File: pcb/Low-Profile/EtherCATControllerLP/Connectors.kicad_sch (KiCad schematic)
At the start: 20 parts, among them J1 FH41-40S-0.5SH_05_, J2 Right Angle 1x4, J3 Conn_01x04_Socket, J4 TYPE-C-31-M-12

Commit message: checkpoint
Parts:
- J1: LCSC Part # (none) -> C596805; LCSC Part Number C596805 -> (none)
- J2: LCSC Part # (none) -> C91552; LCSC Part Number C91552 -> (none)
- J4: LCSC Part # (none) -> C165948; LCSC Part Number C165948 -> (none)
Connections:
- net VDD is gone; now on net VCC: JP1.2 (B)
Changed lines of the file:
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@@
 			)
 		)
-		(property "LCSC Part Number" "C165948"
+		(property "LCSC Part #" "C165948"
 			(at 73.66 157.48 0)
 			(effects
@@
 			)
 		)
-		(property "LCSC Part Number" "C596805"
+		(property "LCSC Part #" "C596805"
 			(at 209.55 86.36 0)
 			(effects
@@
 			)
 		)
-		(property "LCSC Part Number" " C91552"
+		(property "LCSC Part #" " C91552"
 			(at 114.3 125.984 0)
 			(effects
@@
 			)
 		)
-		(property "Value" "VDD"
-			(at 106.68 34.29 0)
-			(effects
-				(font
-					(size 1.27 1.27)
-				)
-			)
-		)
+		(property "Value" "VCC"
+			(at 109.22 38.0999 0)
+			(effects
+				(font
+					(size 1.27 1.27)
+				)
+				(justify left)
+			)
+		)

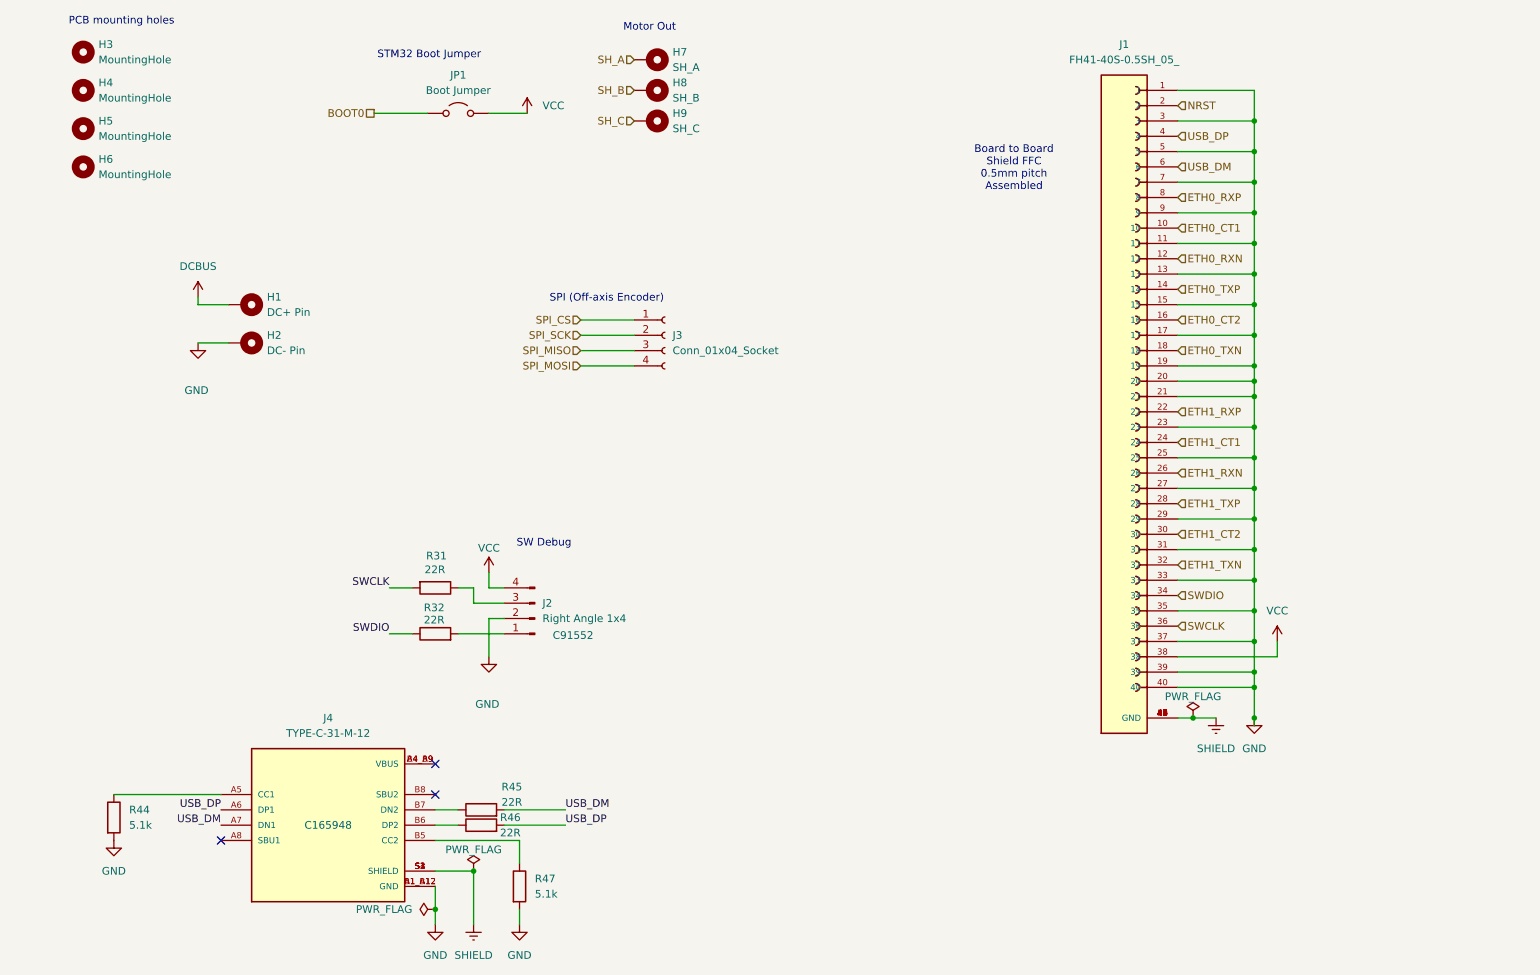
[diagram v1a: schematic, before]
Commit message: Checkpoint changes before switching to XMC4800
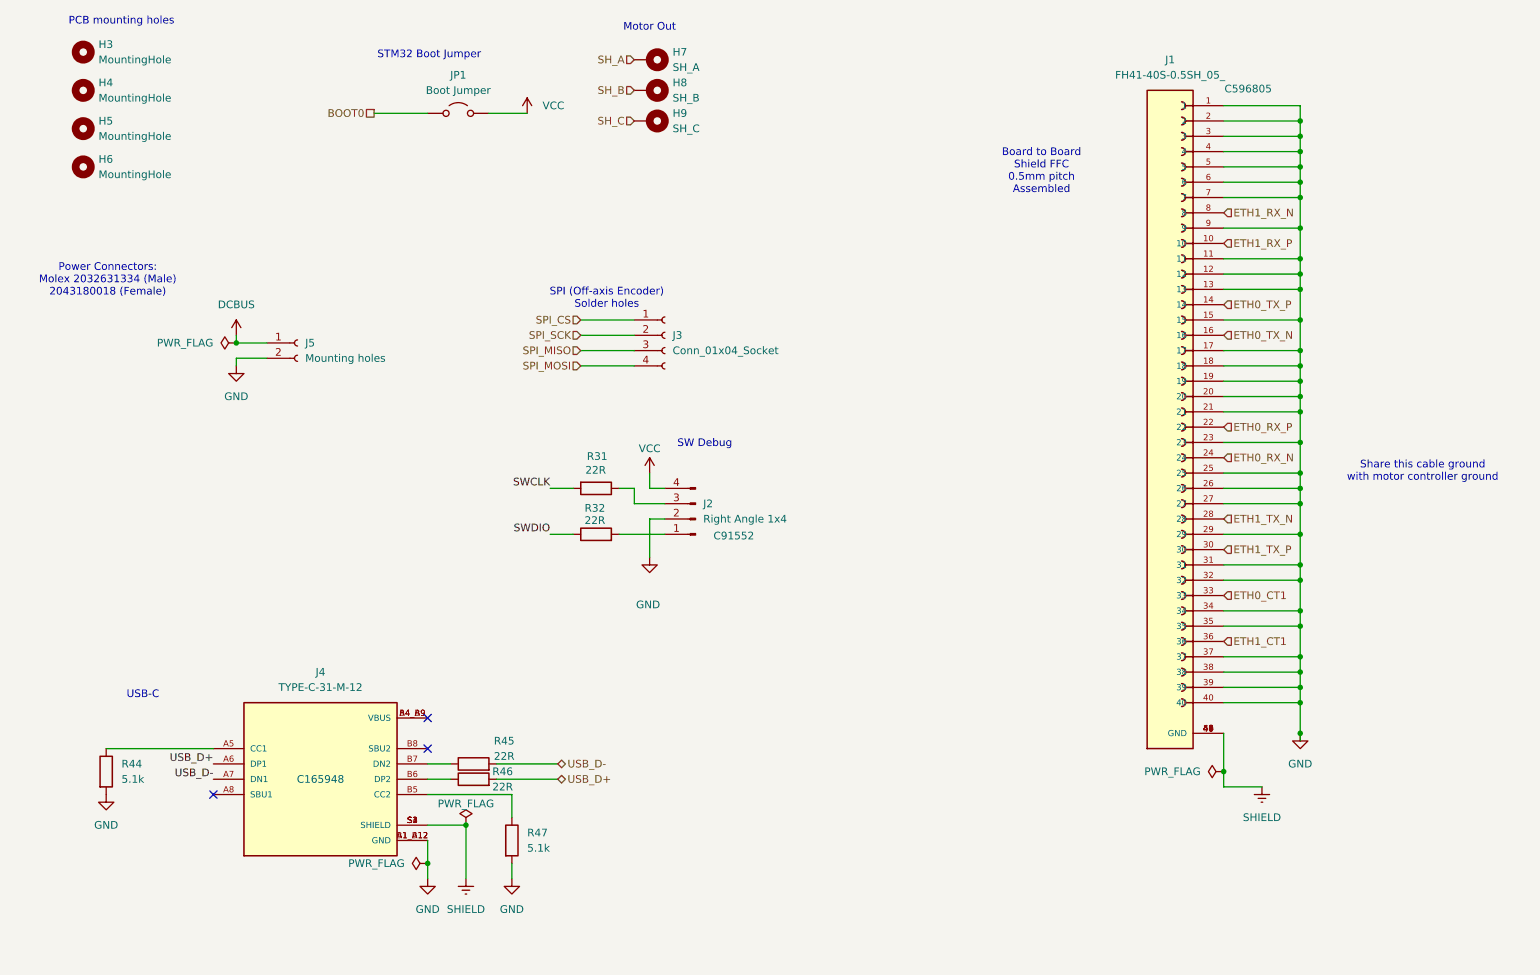
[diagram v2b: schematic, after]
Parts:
- removed H1: DC+ Pin, symbol Mechanical:MountingHole_Pad
- removed H2: DC- Pin, symbol Mechanical:MountingHole_Pad
- added J5: Mounting holes, holes:Dual Post, symbol Connector:Conn_01x02_Socket
- J1: footprint FH41-40S-0.5SH_05_:HRS_FH41-40S-0.5SH_05_ -> FH41:HRS_FH41-40S-0.5SH_05_
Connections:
- net ETH0_RXN is gone; now on net GND: J1.12
- net ETH0_TXN is gone; now on net GND: J1.18
- net ETH1_RXN is gone; now on net GND: J1.26
- net ETH1_TXN is gone; now on net GND: J1.32
- net NRST is gone; now on net GND: J1.2
- net DCBUS: now also J5.1 (Pin_1)
- net ETH0_CT1: now also J1.33; no longer J1.10
- net ETH1_CT1: now also J1.36; no longer J1.24
- net GND: now also J1.34, J1.38, J1.4, J1.6, J5.2 (Pin_2); no longer J1.33
- net SWCLK: no longer J1.36
- net SWDIO: no longer J1.34
- net VCC: no longer J1.38
- net ETH0_CT2 renamed ETH0_TX_N
- net ETH0_RXP renamed ETH1_RX_N
- net ETH0_TXP renamed ETH0_TX_P
- net ETH1_CT2 renamed ETH1_TX_P
- net ETH1_RXP renamed ETH0_RX_P
- net ETH1_TXP renamed ETH1_TX_N
- net USB_DM renamed USB_D-
- net USB_D-: no longer J1.6
- net USB_DP renamed USB_D+
- net USB_D+: no longer J1.4
- new net ETH0_RX_N: J1.24
- new net ETH1_RX_P: J1.10
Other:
- note added: "Power Connectors: Molex 2032631334 (Male) 2043180018 (Female)"
- note added: "SPI (Off-axis Encoder) Solder holes"
- note added: "Share this cable ground with motor controller ground"
- note added: "USB-C"
- note removed: "SPI (Off-axis Encoder)"
- moved on the sheet: J2, J4, R31, R32, R44, R45, R46, R47

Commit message: Finished new 2+2 IOboard
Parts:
- R31, R32, R45, R46: LCSC Part # (none) -> C107701
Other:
- note added: "Power connectors using Samtec UMPT-02/UMPS-02"
- note removed: "Power Connectors: Molex 2032631334 (Male) 2043180018 (Female)"
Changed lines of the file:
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@@
+		)
+	)
+	(text "Power connectors using\nSamtec UMPT-02/UMPS-02"
+		(exclude_from_sim no)
+		(at 36.322 70.104 0)
+		(effects
+			(font
+				(size 1.27 1.27)
+			)
 		)
 	)
@@
 		(exclude_from_sim no)
 		(at 136.144 94.234 0)
-		(effects
-			(font
-				(size 1.27 1.27)
-			)
-		)
-	)
-	(text "Power Connectors:\nMolex 2032631334 (Male)\n2043180018 (Female)"
-		(exclude_from_sim no)
-		(at 37.084 67.056 0)
 		(effects
 			(font
@@
 			)
 		)
+		(property "LCSC Part #" "C107701"
+			(at 97.79 147.32 0)
+			(effects
+				(font
+					(size 1.27 1.27)
+				)
+				(hide yes)
+			)
+		)
 		(pin "1"
 		)
@@
 			)
 		)
+		(property "LCSC Part #" "C107701"
+			(at 118.11 101.6 0)
+			(effects
+				(font
+					(size 1.27 1.27)
+				)
+				(hide yes)
+			)
+		)
 		(pin "2"
 		)
@@
 			)
 		)
+		(property "LCSC Part #" "C107701"
+			(at 118.11 109.22 0)
+			(effects
+				(font
+					(size 1.27 1.27)
+				)
+				(hide yes)
+			)
+		)
 		(pin "1"
 		)
@@
 			(at 97.79 149.86 0)
 			(effects
+				(font
+					(size 1.27 1.27)
+				)
+				(hide yes)
+			)
+		)
+		(property "LCSC Part #" "C107701"
+			(at 97.79 149.86 0)
+			(effects

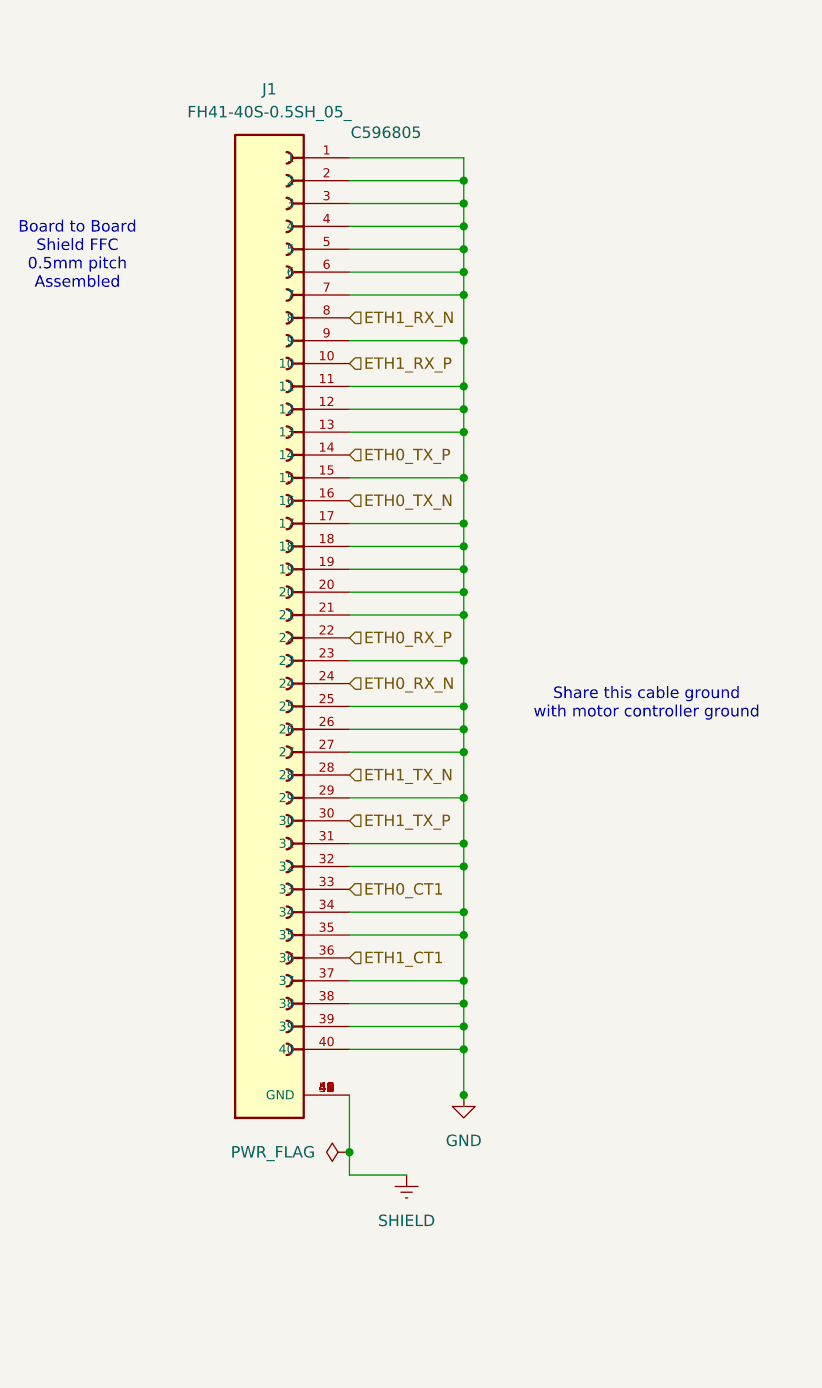
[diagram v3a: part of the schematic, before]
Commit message: Added XMC4800
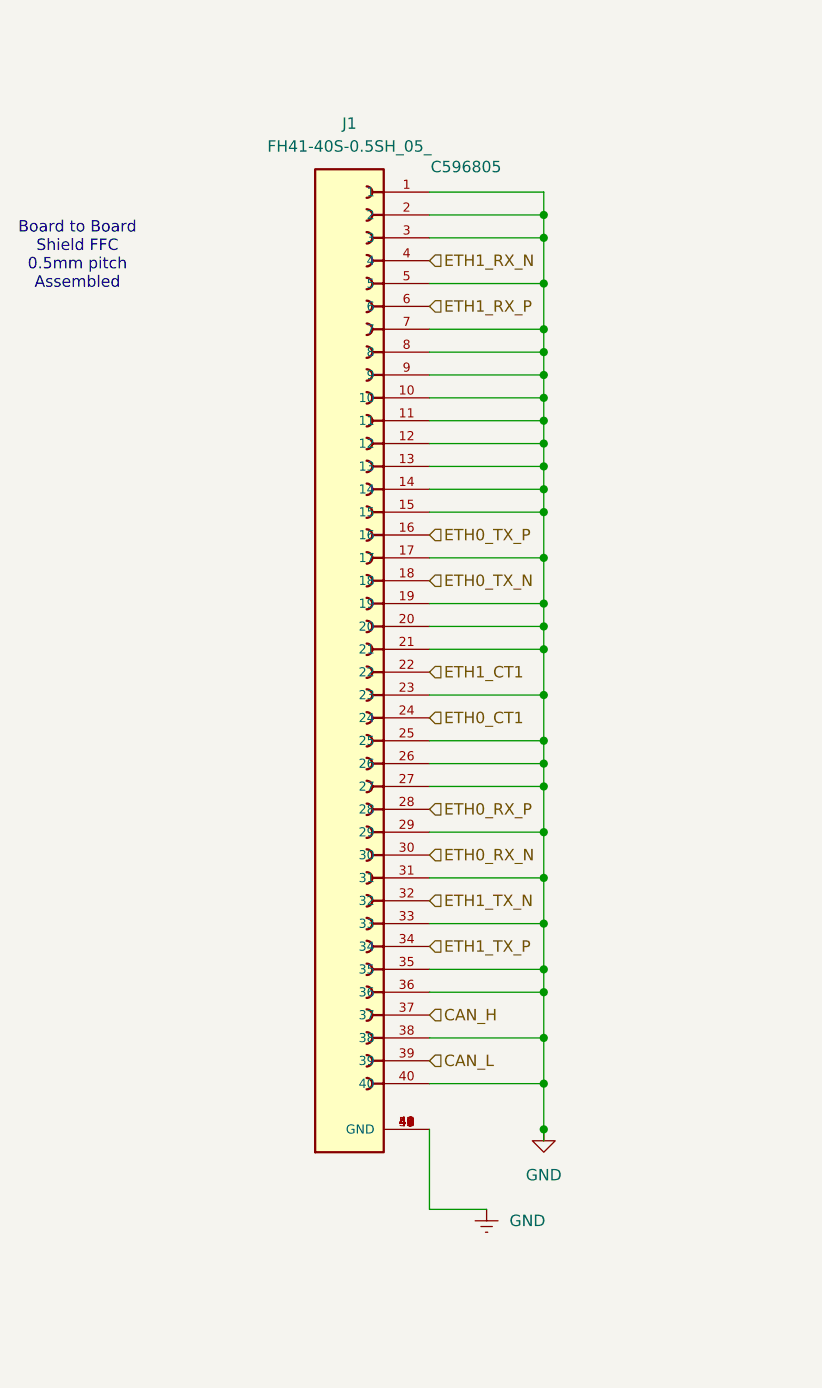
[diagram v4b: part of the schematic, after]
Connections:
- net ETH0_CT1: now also J1.24; no longer J1.33
- net ETH0_RX_N: now also J1.30; no longer J1.24
- net ETH0_RX_P: now also J1.28; no longer J1.22
- net ETH0_TX_N: now also J1.18; no longer J1.16
- net ETH0_TX_P: now also J1.16; no longer J1.14
- net ETH1_CT1: now also J1.22; no longer J1.36
- net ETH1_RX_N: now also J1.4; no longer J1.8
- net ETH1_RX_P: now also J1.6; no longer J1.10
- net ETH1_TX_N: now also J1.32; no longer J1.28
- net ETH1_TX_P: now also J1.34; no longer J1.30
- net GND: now also J1.10, J1.14, J1.33, J1.36, J1.41 (GND), J1.42 (GND), J1.43 (GND), J1.44 (GND), J1.45 (GND), J1.46 (GND), J1.47 (GND), J1.48 (GND), J1.49 (GND), J1.50 (GND), J1.8; no longer J1.18, J1.32, J1.34, J1.37, J1.39, J1.4, J1.6
- net SHIELD: no longer J1.41 (GND), J1.42 (GND), J1.43 (GND), J1.44 (GND), J1.45 (GND), J1.46 (GND), J1.47 (GND), J1.48 (GND), J1.49 (GND), J1.50 (GND)
- new net CAN_H: J1.37
- new net CAN_L: J1.39
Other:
- note removed: "Share this cable ground with motor controller ground"

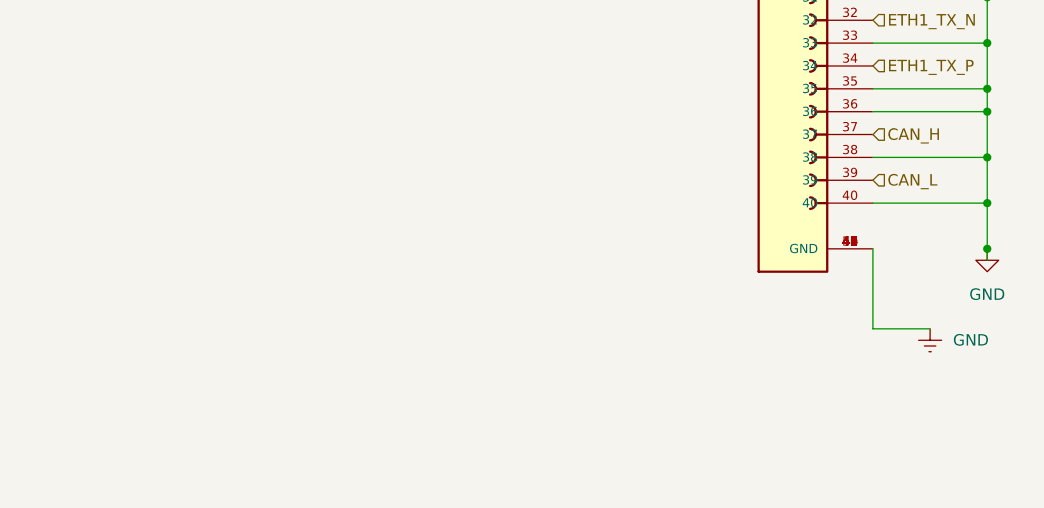
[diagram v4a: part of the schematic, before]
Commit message: Added Ethernet PHY
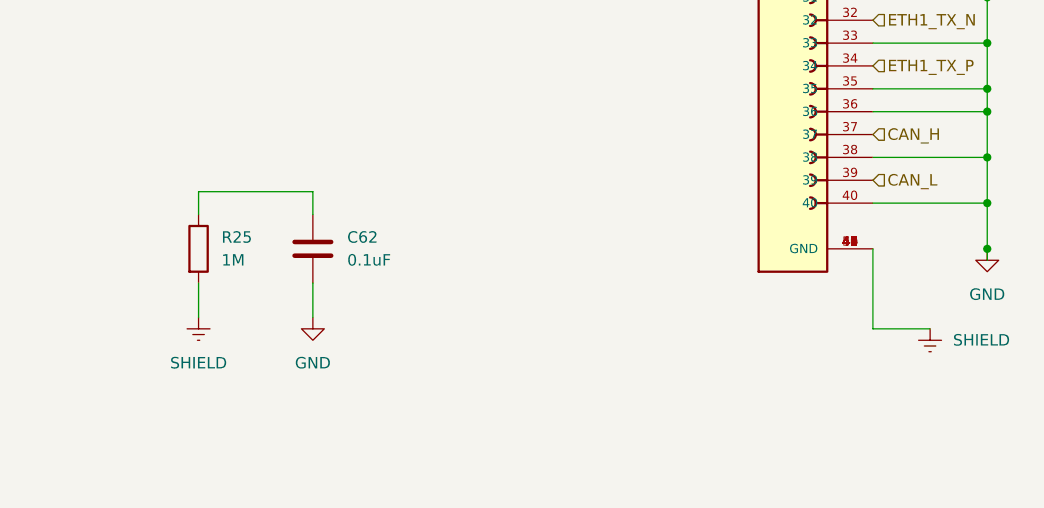
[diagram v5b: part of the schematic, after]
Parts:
- added C62: 0.1uF, symbol Device:C
- added R25: 1M, symbol Device:R
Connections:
- net GND: now also C62.2; no longer J1.41 (GND), J1.42 (GND), J1.43 (GND), J1.44 (GND), J1.45 (GND), J1.46 (GND), J1.47 (GND), J1.48 (GND), J1.49 (GND), J1.50 (GND)
- net SHIELD: now also J1.41 (GND), J1.42 (GND), J1.43 (GND), J1.44 (GND), J1.45 (GND), J1.46 (GND), J1.47 (GND), J1.48 (GND), J1.49 (GND), J1.50 (GND), R25.2
- new net: C62.1, R25.1
